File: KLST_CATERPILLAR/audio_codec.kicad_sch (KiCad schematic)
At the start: 43 parts, among them J16 MIC_IN, J17 LINE_IN, J18 HEADPHONE_OUT+MIC, J19 LINE_OUT, U13 WM8904CGEFL/V

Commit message: finished placing components
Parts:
- removed C59: 470pF, Capacitor_SMD:C_0402_1005Metric, symbol Device:C_Small
- removed C62: 1uF, Capacitor_SMD:C_0402_1005Metric, symbol Device:C_Small
- removed FB3: 5Ω@100MHz, Inductor_SMD:L_0402_1005Metric, symbol Device:FerriteBead_Small
- removed J16: MIC_IN, PJ-316A-6A:PJ-316A-6A, symbol Connector_Audio:AudioJack4_SwitchTR1
- removed R76: 2.2K, Resistor_SMD:R_0603_1608Metric, symbol Device:R_Small
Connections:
- net (MIC_IN_LEFT) renamed MIC_IN_MONO
- no-connect marks 12 -> 9
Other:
- moved on the sheet: C58, C61, FB2, R75

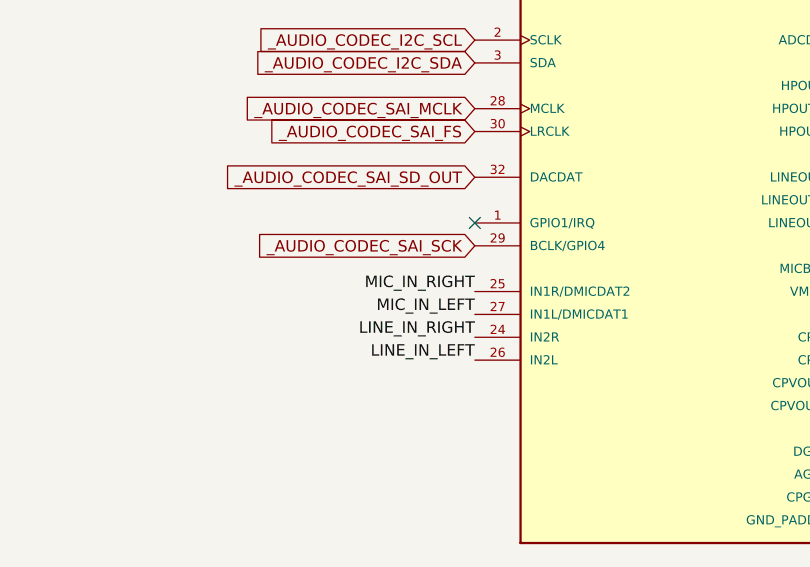
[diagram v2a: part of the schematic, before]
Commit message: routed modules ( not finished )
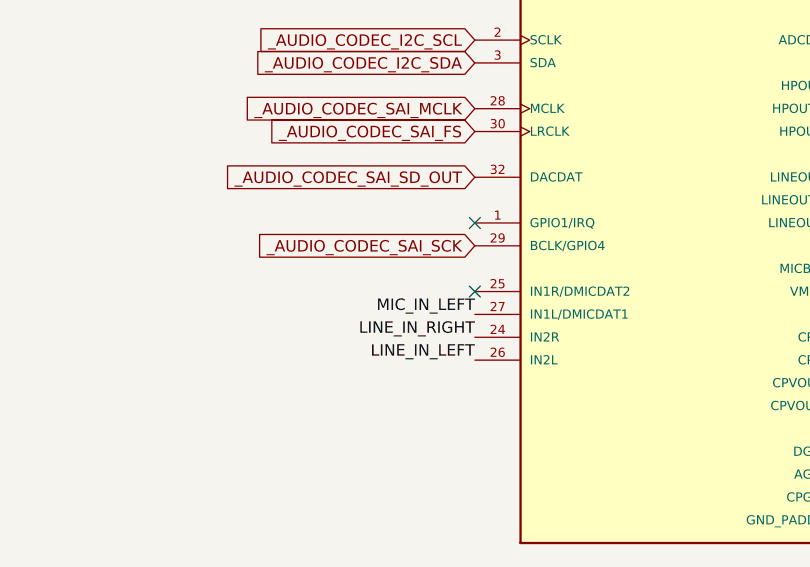
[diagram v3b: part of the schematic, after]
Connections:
- net MIC_IN_RIGHT: no longer names the net of U13.25 (IN1R/DMICDAT2)
- no-connect marks 9 -> 10
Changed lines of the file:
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@@
+	)
+	(no_connect
+		(at 110.49 90.805)
 	)
 	(no_connect
@@
 		)
 	)
-	(label "MIC_IN_RIGHT"
-		(at 110.49 90.805 180)
-		(fields_autoplaced yes)
-		(effects
-			(font
-				(size 1.27 1.27)
-			)
-			(justify right bottom)
-		)
-	)

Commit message: added test points, replaced unavailable components
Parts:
- R75: footprint Resistor_SMD:R_0603_1608Metric -> Resistor_SMD:R_0402_1005Metric; JLCPCB C101304 -> C966835
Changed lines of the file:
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@@
 			)
 		)
-		(property "Footprint" "Resistor_SMD:R_0603_1608Metric"
+		(property "Footprint" "Resistor_SMD:R_0402_1005Metric"
 			(at 140.97 157.48 0)
 			(effects
@@
 			)
 		)
-		(property "JLCPCB" "C101304"
+		(property "JLCPCB" "C966835"
 			(at 140.97 157.48 0)
 			(effects
